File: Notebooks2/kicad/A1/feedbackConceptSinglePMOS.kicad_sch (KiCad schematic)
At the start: 15 parts

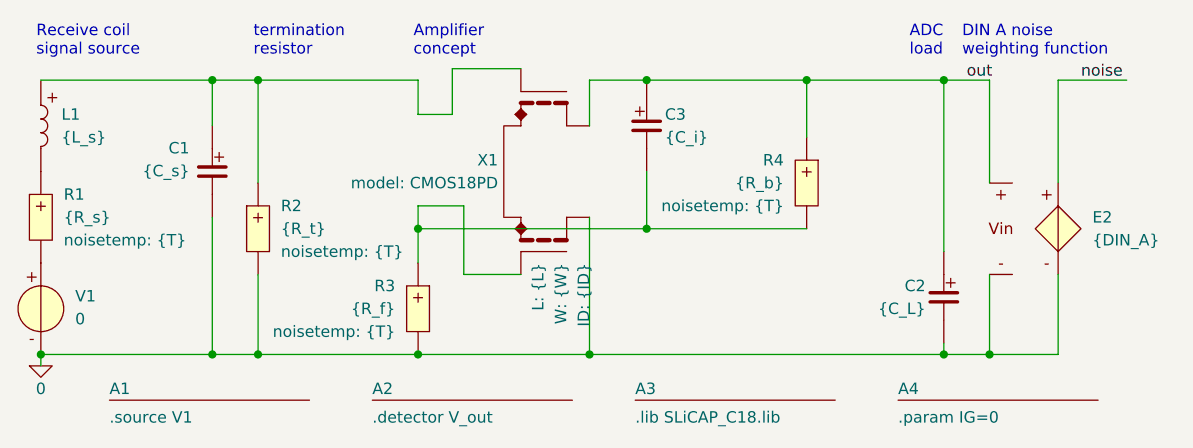
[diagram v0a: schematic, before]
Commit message: Add fumo.net and update sym-lib-table and biasP.net
- Created a new netlist file `fumo.net` for the circuit design, including components such as capacitors, resistors, inductors, and voltage sources with appropriate properties and connections.
- Updated the `sym-lib-table` to point to the correct URI for the SLiCAP library.
- Modified the date in `biasP.net` to reflect the latest changes made to the design.
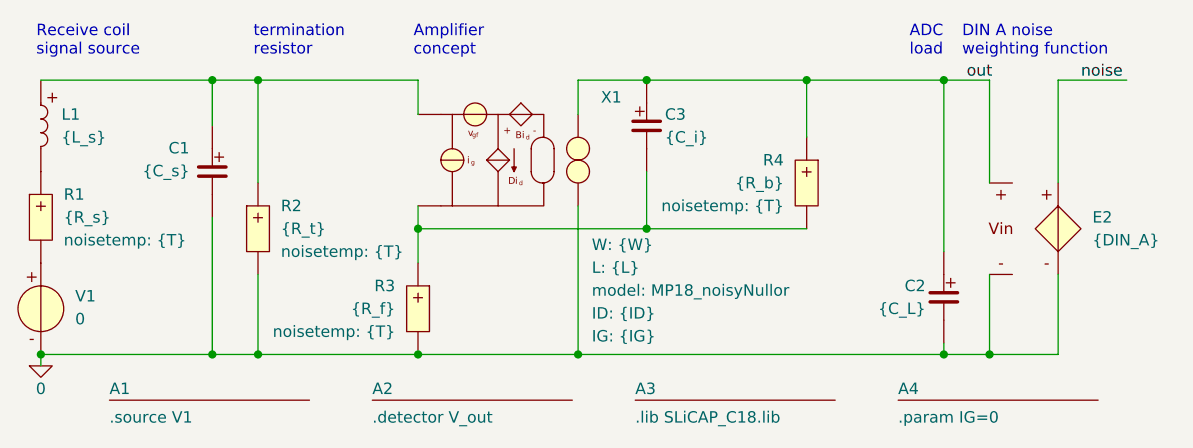
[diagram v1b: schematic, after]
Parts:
- removed X1: ~, symbol SLiCAP:XMD
- added X1: ~, symbol SLiCAP:XM_noisyNullor
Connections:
- net 0: now also X1.2 (outN)
- net out: now also X1.1 (outP)
- net at C3.2, R3.1, R4.2: now also X1.4 (inN)
- net at C1.1, L1.1, R2.1: now also X1.3 (inP)
